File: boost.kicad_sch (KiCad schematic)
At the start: 24 parts, among them Q5 BSC059N04LS6, Q6 BSC059N04LS6, U7 LM5123-Q1

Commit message: Finalized design !!!
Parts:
- removed L2: 1.3u, symbol Device:L_Iron
- added C74: 0.1u, Capacitor_SMD:C_0603_1608Metric_Pad1.08x0.95mm_HandSolder, symbol Device:C
- added L7: 1.5u, Inductor_SMD:L_Bourns_SRP1245A, symbol Device:L_Ferrite
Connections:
- net CSN: now also L7.1
- net GNDPWR: now also C74.2
- net OUT: now also C74.1
- net SW: now also L7.2
- net HO_R: now reaches Q5.4 (G), R33.1
- net LO_R: now reaches Q6.4 (G), R35.1
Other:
- note added: "(+local cap)"
- moved on the sheet: C20, C21, C22, C23, C24, C25, Q5, Q6, R33, R34, R35, R39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

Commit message: Adjusted some things + changed discharge to have a smaller time constant
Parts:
- R41: Mouser Part Number (none) -> 603-RT0603BRD07280KL
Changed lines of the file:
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@@
+			)
+		)
+		(property "Mouser Part Number" "603-RT0603BRD07280KL"
+			(at 52.07 124.46 0)
+			(effects
+				(font
+					(size 1.27 1.27)
+				)
+				(hide yes)
 			)
 		)

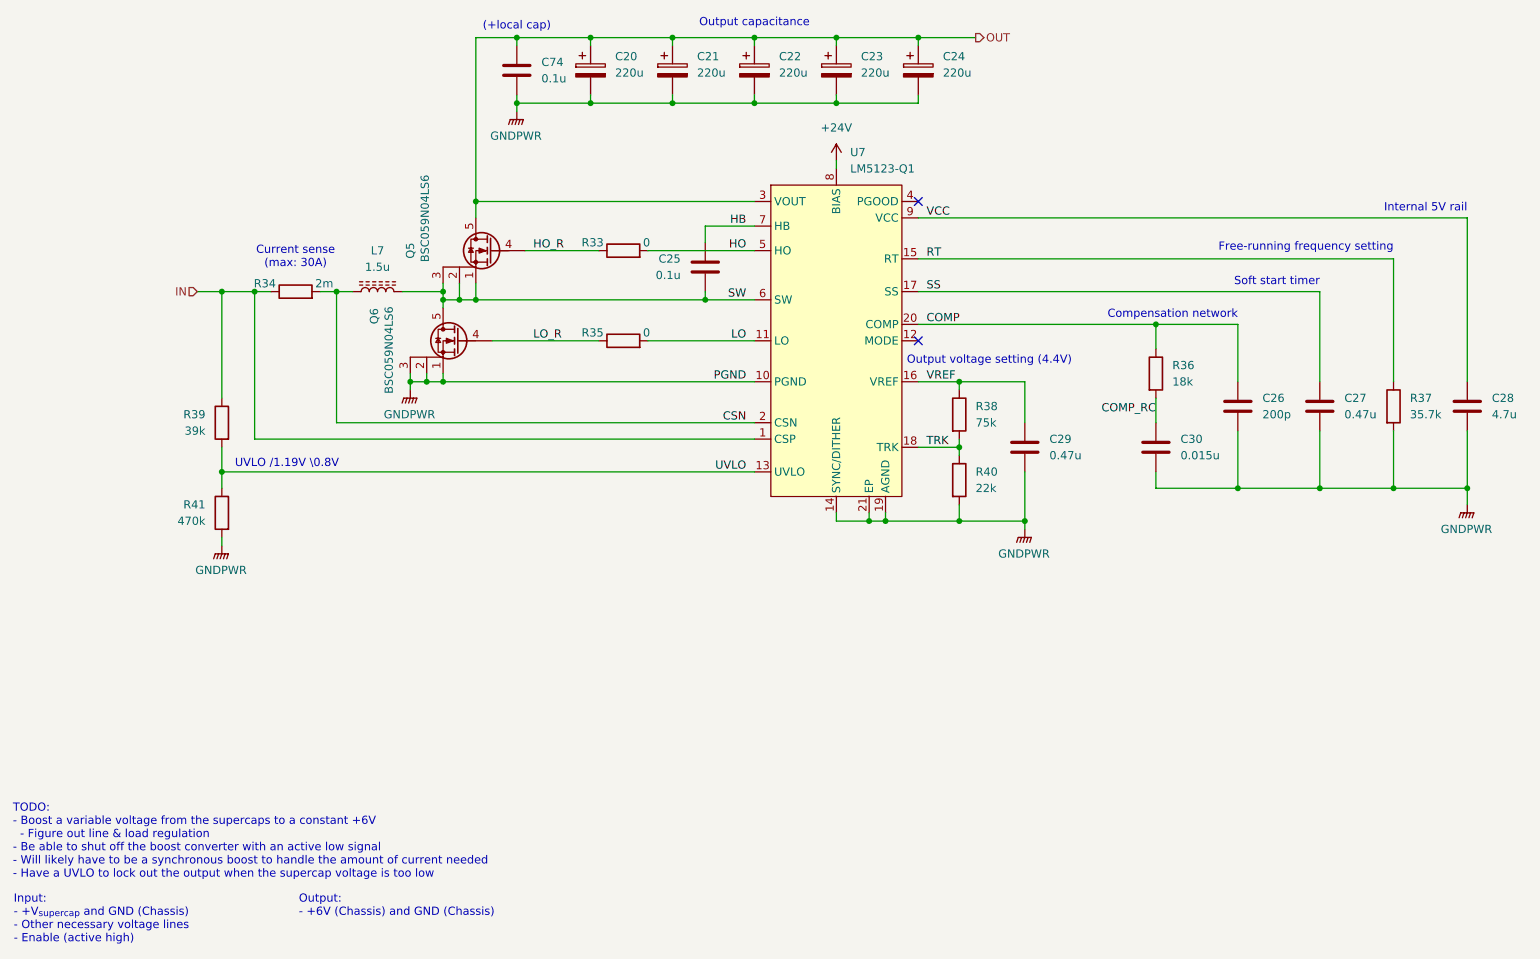
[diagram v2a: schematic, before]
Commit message: Renumbering components
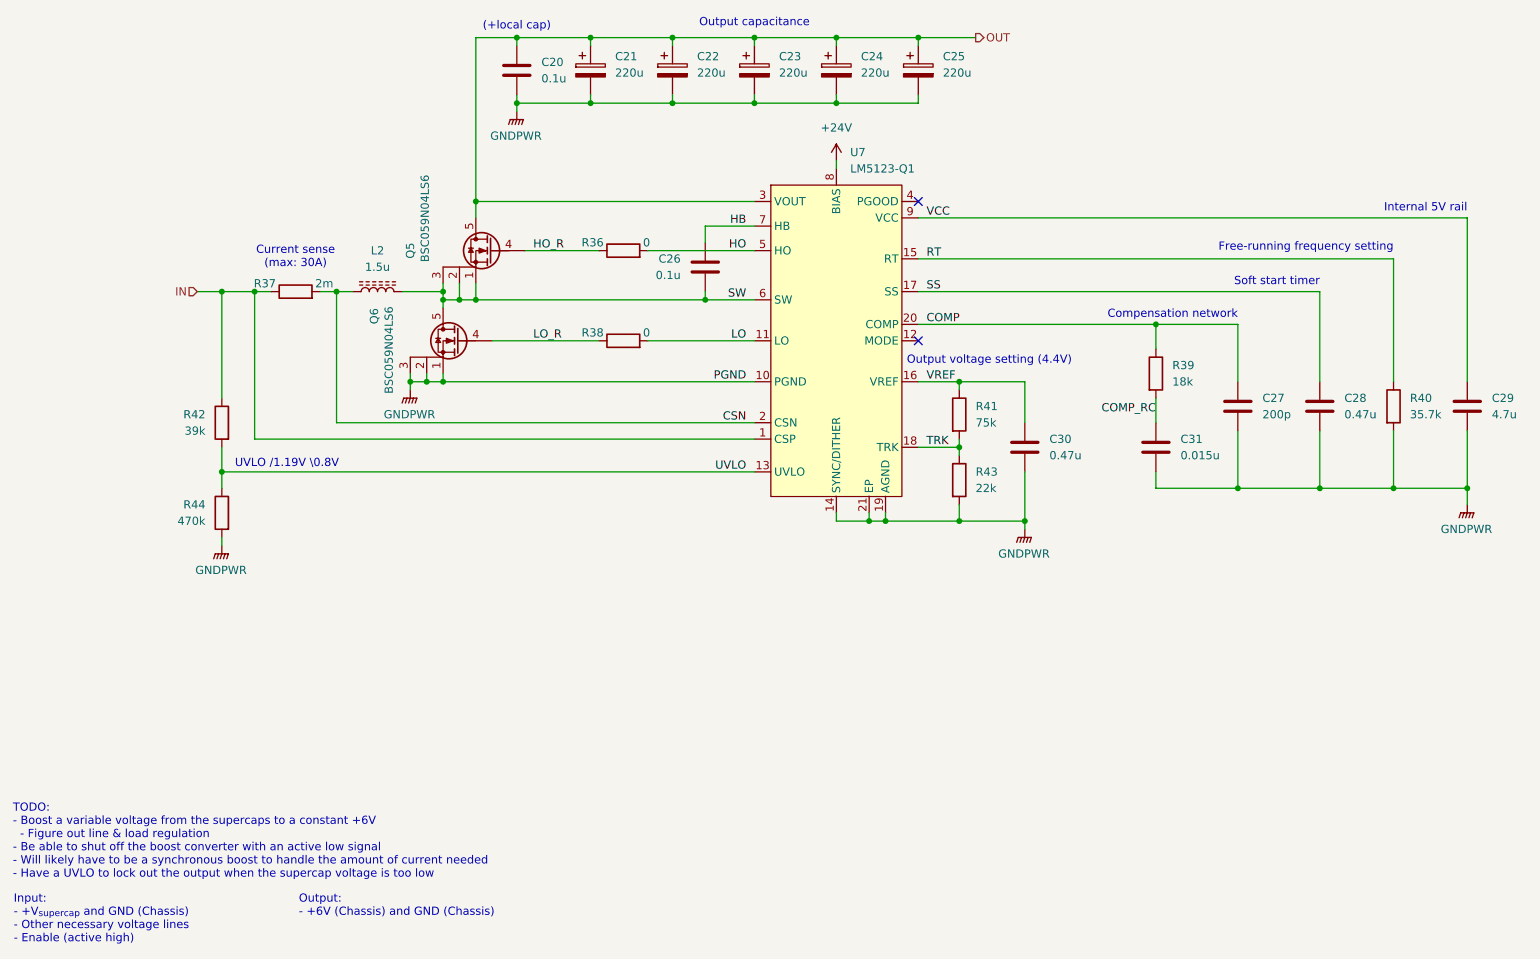
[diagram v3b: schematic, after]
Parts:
- renumbered C74 to C20, C20 to C21, C21 to C22, C22 to C23, C23 to C24, C24 to C25, C25 to C26, C26 to C27, C27 to C28, C28 to C29, C29 to C30, C30 to C31, L7 to L2, R33 to R36, R34 to R37, R35 to R38, R36 to R39, R37 to R40, R38 to R41, R39 to R42, R40 to R43, R41 to R44
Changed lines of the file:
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@@
 		(on_board yes)
 		(dnp no)
-		(property "Reference" "R41"
+		(property "Reference" "R44"
 			(at 49.53 123.1899 0)
 			(effects
@@
 			(project "SupercapManager"
 				(path "/6197145b-e7d4-44cc-9d90-537b6501bf60/fd749e99-bd1e-4aca-86d6-8b572dc00b7d"
-					(reference "R41")
+					(reference "R44")
 					(unit 1)
 				)
@@
 		(dnp no)
 		(fields_autoplaced yes)
-		(property "Reference" "C22"
+		(property "Reference" "C23"
 			(at 138.43 53.7209 0)
 			(effects
@@
 			(project "SupercapManager"
 				(path "/6197145b-e7d4-44cc-9d90-537b6501bf60/fd749e99-bd1e-4aca-86d6-8b572dc00b7d"
-					(reference "C22")
+					(reference "C23")
 					(unit 1)
 				)
@@
 		(dnp no)
 		(fields_autoplaced yes)
-		(property "Reference" "#PWR050"
+		(property "Reference" "#PWR051"
 			(at 245.11 128.27 0)
 			(effects
@@
 			(project "SupercapManager"
 				(path "/6197145b-e7d4-44cc-9d90-537b6501bf60/fd749e99-bd1e-4aca-86d6-8b572dc00b7d"
-					(reference "#PWR050")
+					(reference "#PWR051")
 					(unit 1)
 				)
@@
 		(on_board yes)
 		(dnp no)
-		(property "Reference" "C28"
+		(property "Reference" "C29"
 			(at 248.92 106.6799 0)
 			(effects
@@
 			(project "SupercapManager"
 				(path "/6197145b-e7d4-44cc-9d90-537b6501bf60/fd749e99-bd1e-4aca-86d6-8b572dc00b7d"
-					(reference "C28")
+					(reference "C29")
 					(unit 1)
 				)
@@
 		(dnp no)
 		(fields_autoplaced yes)
-		(property "Reference" "C20"
+		(property "Reference" "C21"
 			(at 113.03 53.7209 0)
 			(effects
@@
 			(project ""
 				(path "/6197145b-e7d4-44cc-9d90-537b6501bf60/fd749e99-bd1e-4aca-86d6-8b572dc00b7d"
-					(reference "C20")
+					(reference "C21")
 					(unit 1)
 				)
@@
 		(dnp no)
 		(fields_autoplaced yes)
-		(property "Reference" "#PWR051"
+		(property "Reference" "#PWR052"
 			(at 176.53 132.08 0)
 			(effects
@@
 			(project ""
 				(path "/6197145b-e7d4-44cc-9d90-537b6501bf60/fd749e99-bd1e-4aca-86d6-8b572dc00b7d"
-					(reference "#PWR051")
+					(reference "#PWR052")
 					(unit 1)
 				)
@@
 		(on_board yes)
 		(dnp no)
-		(property "Reference" "R37"
+		(property "Reference" "R40"
 			(at 236.22 106.6799 0)
 			(effects
@@
 			(project "SupercapManager"
 				(path "/6197145b-e7d4-44cc-9d90-537b6501bf60/fd749e99-bd1e-4aca-86d6-8b572dc00b7d"
-					(reference "R37")
+					(reference "R40")
 					(unit 1)
 				)
@@
 		(on_board yes)
 		(dnp no)
-		(property "Reference" "C26"
+		(property "Reference" "C27"
 			(at 213.36 106.6799 0)
 			(effects
@@
 			(project "SupercapManager"
 				(path "/6197145b-e7d4-44cc-9d90-537b6501bf60/fd749e99-bd1e-4aca-86d6-8b572dc00b7d"
-					(reference "C26")
+					(reference "C27")
 					(unit 1)
 				)
@@
 		(on_board yes)
 		(dnp no)
-		(property "Reference" "R39"
+		(property "Reference" "R42"
 			(at 49.53 109.2199 0)
 			(effects
@@
 			(project ""
 				(path "/6197145b-e7d4-44cc-9d90-537b6501bf60/fd749e99-bd1e-4aca-86d6-8b572dc00b7d"
-					(reference "R39")
+					(reference "R42")
 					(unit 1)
 				)
@@
 		(on_board yes)
 		(dnp no)
-		(property "Reference" "R33"
+		(property "Reference" "R36"
 			(at 111.252 83.312 90)
 			(effects
@@
 			(project "SupercapManager"
 				(path "/6197145b-e7d4-44cc-9d90-537b6501bf60/fd749e99-bd1e-4aca-86d6-8b572dc00b7d"
-					(reference "R33")
+					(reference "R36")
 					(unit 1)
 				)
@@
 		(on_board yes)
 		(dnp no)
-		(property "Reference" "R35"
+		(property "Reference" "R38"
 			(at 111.252 97.282 90)
 			(effects
@@
 			(project "SupercapManager"
 				(path "/6197145b-e7d4-44cc-9d90-537b6501bf60/fd749e99-bd1e-4aca-86d6-8b572dc00b7d"
-					(reference "R35")
+					(reference "R38")
 					(unit 1)
 				)
@@
 		(dnp no)
 		(fields_autoplaced yes)
-		(property "Reference" "C24"
+		(property "Reference" "C25"
 			(at 163.83 53.7209 0)
 			(effects
@@
 			(project "SupercapManager"
 				(path "/6197145b-e7d4-44cc-9d90-537b6501bf60/fd749e99-bd1e-4aca-86d6-8b572dc00b7d"
-					(reference "C24")
+					(reference "C25")
 					(unit 1)
 				)
@@
 		(on_board yes)
 		(dnp no)
-		(property "Reference" "R34"
+		(property "Reference" "R37"
 			(at 60.452 89.662 90)
 			(effects
@@
 			(project "SupercapManager"
 				(path "/6197145b-e7d4-44cc-9d90-537b6501bf60/fd749e99-bd1e-4aca-86d6-8b572dc00b7d"
-					(reference "R34")
+					(reference "R37")
 					(unit 1)
 				)
@@
 		(on_board yes)
 		(dnp no)
-		(property "Reference" "C27"
+		(property "Reference" "C28"
 			(at 226.06 106.6799 0)
 			(effects
@@
 			(project "SupercapManager"
 				(path "/6197145b-e7d4-44cc-9d90-537b6501bf60/fd749e99-bd1e-4aca-86d6-8b572dc00b7d"
-					(reference "C27")
+					(reference "C28")
 					(unit 1)
 				)
@@
 		(on_board yes)
 		(dnp no)
-		(property "Reference" "C30"
+		(property "Reference" "C31"
 			(at 200.66 113.0299 0)
 			(effects
@@
 			(project "SupercapManager"
 				(path "/6197145b-e7d4-44cc-9d90-537b6501bf60/fd749e99-bd1e-4aca-86d6-8b572dc00b7d"
-					(reference "C30")
+					(reference "C31")
 					(unit 1)
 				)
@@
 		(on_board yes)
 		(dnp no)
-		(property "Reference" "R40"
+		(property "Reference" "R43"
 			(at 168.91 118.1099 0)
 			(effects
@@
 			(project "SupercapManager"
 				(path "/6197145b-e7d4-44cc-9d90-537b6501bf60/fd749e99-bd1e-4aca-86d6-8b572dc00b7d"
-					(reference "R40")
+					(reference "R43")
 					(unit 1)
 				)
@@
 		(dnp no)
 		(fields_autoplaced yes)
-		(property "Reference" "C21"
+		(property "Reference" "C22"
 			(at 125.73 53.7209 0)
 			(effects
@@
 			(project "SupercapManager"
 				(path "/6197145b-e7d4-44cc-9d90-537b6501bf60/fd749e99-bd1e-4aca-86d6-8b572dc00b7d"
-					(reference "C21")
+					(reference "C22")
 					(unit 1)
 				)
@@
 		(on_board yes)
 		(dnp no)
-		(property "Reference" "R36"
+		(property "Reference" "R39"
 			(at 199.39 101.5999 0)
 			(effects
@@
 			(project "SupercapManager"
 				(path "/6197145b-e7d4-44cc-9d90-537b6501bf60/fd749e99-bd1e-4aca-86d6-8b572dc00b7d"
-					(reference "R36")
+					(reference "R39")
 					(unit 1)
 				)
@@
 		(dnp no)
 		(fields_autoplaced yes)
-		(property "Reference" "#PWR049"
+		(property "Reference" "#PWR050"
 			(at 81.28 110.49 0)
 			(effects
@@
 			(project "SupercapManager"
 				(path "/6197145b-e7d4-44cc-9d90-537b6501bf60/fd749e99-bd1e-4aca-86d6-8b572dc00b7d"
-					(reference "#PWR049")
+					(reference "#PWR050")
 					(unit 1)
 				)
@@
 		(on_board yes)
 		(dnp no)
-		(property "Reference" "C29"
+		(property "Reference" "C30"
 			(at 180.34 113.0299 0)
 			(effects
@@
 			(project "SupercapManager"
 				(path "/6197145b-e7d4-44cc-9d90-537b6501bf60/fd749e99-bd1e-4aca-86d6-8b572dc00b7d"
-					(reference "C29")
+					(reference "C30")
 					(unit 1)
 				)
@@
 		(dnp no)
 		(fields_autoplaced yes)
-		(property "Reference" "L7"
+		(property "Reference" "L2"
 			(at 76.2 83.82 90)
 			(effects
@@
 			(project "SupercapManager"
 				(path "/6197145b-e7d4-44cc-9d90-537b6501bf60/fd749e99-bd1e-4aca-86d6-8b572dc00b7d"
-					(reference "L7")
+					(reference "L2")
 					(unit 1)
 				)
@@
 		(on_board yes)
 		(dnp no)
-		(property "Reference" "C25"
+		(property "Reference" "C26"
 			(at 123.19 85.0899 0)
 			(effects
@@
 			(project ""
 				(path "/6197145b-e7d4-44cc-9d90-537b6501bf60/fd749e99-bd1e-4aca-86d6-8b572dc00b7d"
-					(reference "C25")
+					(reference "C26")
 					(unit 1)
 				)
@@
 		(dnp no)
 		(fields_autoplaced yes)
-		(property "Reference" "#PWR052"
+		(property "Reference" "#PWR053"
 			(at 52.07 134.62 0)
 			(effects
@@
 			(project "SupercapManager"
 				(path "/6197145b-e7d4-44cc-9d90-537b6501bf60/fd749e99-bd1e-4aca-86d6-8b572dc00b7d"
-					(reference "#PWR052")
+					(reference "#PWR053")
 					(unit 1)
 				)
@@
 		(dnp no)
 		(fields_autoplaced yes)
-		(property "Reference" "#PWR047"
+		(property "Reference" "#PWR048"
 			(at 97.79 67.31 0)
 			(effects
@@
 			(project "SupercapManager"
 				(path "/6197145b-e7d4-44cc-9d90-537b6501bf60/fd749e99-bd1e-4aca-86d6-8b572dc00b7d"
-					(reference "#PWR047")
+					(reference "#PWR048")
 					(unit 1)
 				)
@@
 		(on_board yes)
 		(dnp no)
-		(property "Reference" "R38"
+		(property "Reference" "R41"
 			(at 168.91 107.9499 0)
 			(effects
@@
 			(project "SupercapManager"
 				(path "/6197145b-e7d4-44cc-9d90-537b6501bf60/fd749e99-bd1e-4aca-86d6-8b572dc00b7d"
-					(reference "R38")
+					(reference "R41")
 					(unit 1)
 				)
@@
 		(dnp no)
 		(fields_autoplaced yes)
-		(property "Reference" "#PWR048"
+		(property "Reference" "#PWR049"
 			(at 147.32 73.66 0)
 			(effects
@@
 			(project ""
 				(path "/6197145b-e7d4-44cc-9d90-537b6501bf60/fd749e99-bd1e-4aca-86d6-8b572dc00b7d"
-					(reference "#PWR048")
+					(reference "#PWR049")
 					(unit 1)
 				)
@@
 		(on_board yes)
 		(dnp no)
-		(property "Reference" "C74"
+		(property "Reference" "C20"
 			(at 101.6 54.6099 0)
 			(effects
@@
 			(project "SupercapManager"
 				(path "/6197145b-e7d4-44cc-9d90-537b6501bf60/fd749e99-bd1e-4aca-86d6-8b572dc00b7d"
-					(reference "C74")
+					(reference "C20")
 					(unit 1)
 				)
@@
 		(dnp no)
 		(fields_autoplaced yes)
-		(property "Reference" "C23"
+		(property "Reference" "C24"
 			(at 151.13 53.7209 0)
 			(effects
@@
 			(project "SupercapManager"
 				(path "/6197145b-e7d4-44cc-9d90-537b6501bf60/fd749e99-bd1e-4aca-86d6-8b572dc00b7d"
-					(reference "C23")
-					(unit 1)
-				)
+					(reference "C24")
+					(unit 1)
+				)

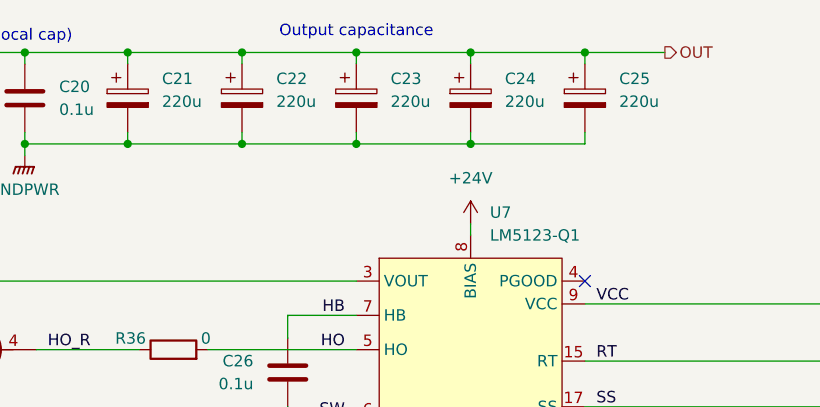
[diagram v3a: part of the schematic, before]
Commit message: Add voltage ratings to capacitors & respec caps to not explode
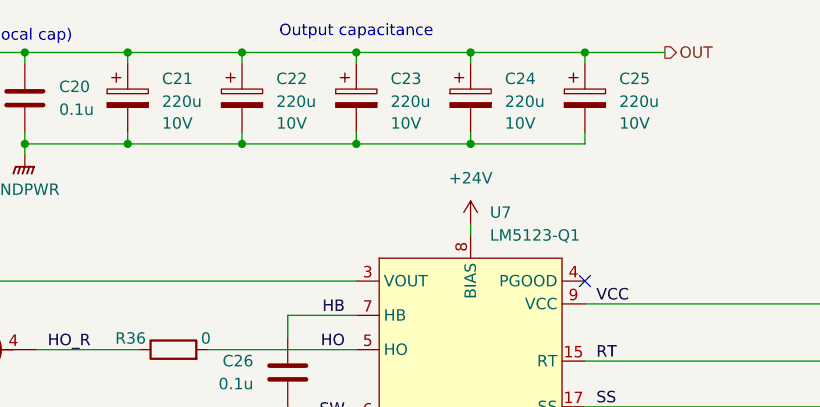
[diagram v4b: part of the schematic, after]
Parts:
- C21, C22, C23, C24, C25: Voltage Rating (none) -> 10V
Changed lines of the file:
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@@
 		(on_board yes)
 		(dnp no)
-		(fields_autoplaced yes)
 		(property "Reference" "C23"
 			(at 138.43 53.7209 0)
@@
 				)
 				(hide yes)
+			)
+		)
+		(property "Voltage Rating" "10V"
+			(at 138.43 58.674 0)
+			(effects
+				(font
+					(size 1.27 1.27)
+				)
+				(justify left)
 			)
 		)
@@
 		(on_board yes)
 		(dnp no)
-		(fields_autoplaced yes)
 		(property "Reference" "C21"
 			(at 113.03 53.7209 0)
@@
 				)
 				(hide yes)
+			)
+		)
+		(property "Voltage Rating" "10V"
+			(at 113.03 58.674 0)
+			(effects
+				(font
+					(size 1.27 1.27)
+				)
+				(justify left)
 			)
 		)
@@
 		(on_board yes)
 		(dnp no)
-		(fields_autoplaced yes)
 		(property "Reference" "C25"
 			(at 163.83 53.7209 0)
@@
 				)
 				(hide yes)
+			)
+		)
+		(property "Voltage Rating" "10V"
+			(at 163.83 58.674 0)
+			(effects
+				(font
+					(size 1.27 1.27)
+				)
+				(justify left)
 			)
 		)
@@
 		(on_board yes)
 		(dnp no)
-		(fields_autoplaced yes)
 		(property "Reference" "C22"
 			(at 125.73 53.7209 0)
@@
 				)
 				(hide yes)
+			)
+		)
+		(property "Voltage Rating" "10V"
+			(at 125.73 58.674 0)
+			(effects
+				(font
+					(size 1.27 1.27)
+				)
+				(justify left)
 			)
 		)
@@
 		(on_board yes)
 		(dnp no)
-		(fields_autoplaced yes)
 		(property "Reference" "C24"
 			(at 151.13 53.7209 0)
@@
 			)
 		)
+		(property "Voltage Rating" "10V"
+			(at 151.13 58.674 0)
+			(effects
+				(font
+					(size 1.27 1.27)
+				)
+				(justify left)
+			)
+		)

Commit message: Sourcing various parts
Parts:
- R37: footprint Resistor_SMD:R_0603_1608Metric_Pad0.98x0.95mm_HandSolder -> Resistor_SMD:R_2512_6332Metric_Pad1.40x3.35mm_HandSolder; Mouser Part Number (none) -> 652-CRF2512FZR002ELF
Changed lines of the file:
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@@
 			)
 		)
-		(property "Footprint" "Resistor_SMD:R_0603_1608Metric_Pad0.98x0.95mm_HandSolder"
+		(property "Footprint" "Resistor_SMD:R_2512_6332Metric_Pad1.40x3.35mm_HandSolder"
 			(at 63.5 91.948 90)
 			(effects
@@
 			)
 		)
-		(property "Datasheet" "~"
+		(property "Datasheet" "https://www.mouser.com/datasheet/2/54/crf-937137.pdf"
 			(at 63.5 90.17 0)
 			(effects
@@
 			)
 		)
+		(property "Mouser Part Number" "652-CRF2512FZR002ELF"
+			(at 63.5 90.17 0)
+			(effects
+				(font
+					(size 1.27 1.27)
+				)
+				(hide yes)
+			)
+		)
